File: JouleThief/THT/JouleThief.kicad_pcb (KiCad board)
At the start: 2 copper layers, 55.3 x 13.2 mm, 11 parts, among them J1 Screw_Terminal_01x02, J2 Screw_Terminal_01x02, Q1 BC547, Q2 BC547

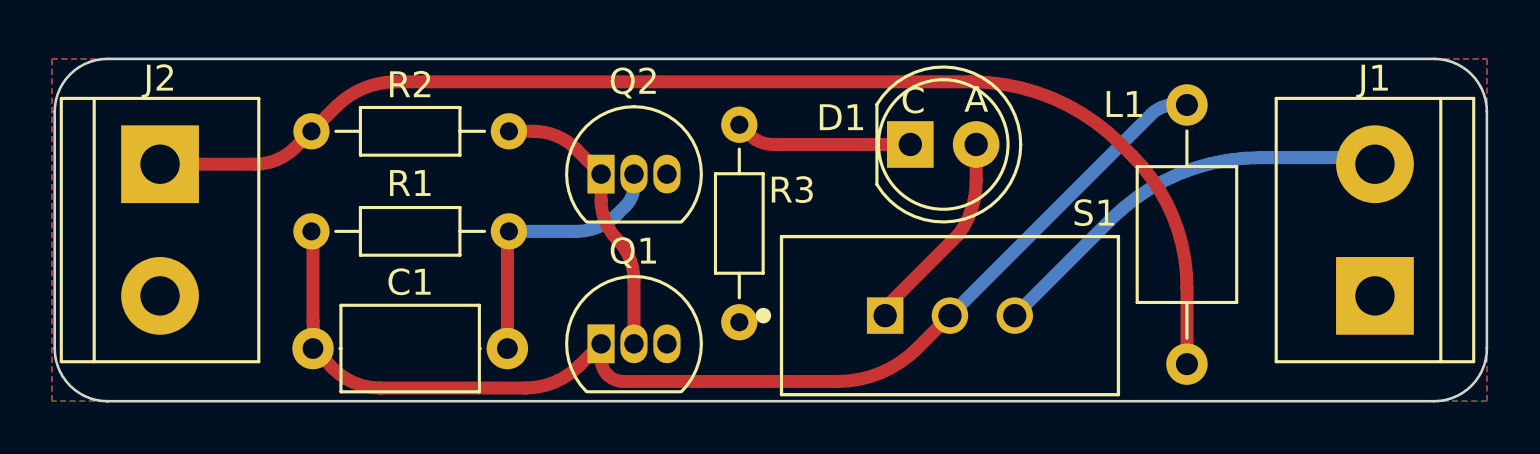
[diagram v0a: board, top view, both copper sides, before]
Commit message: added tht components back tot tht
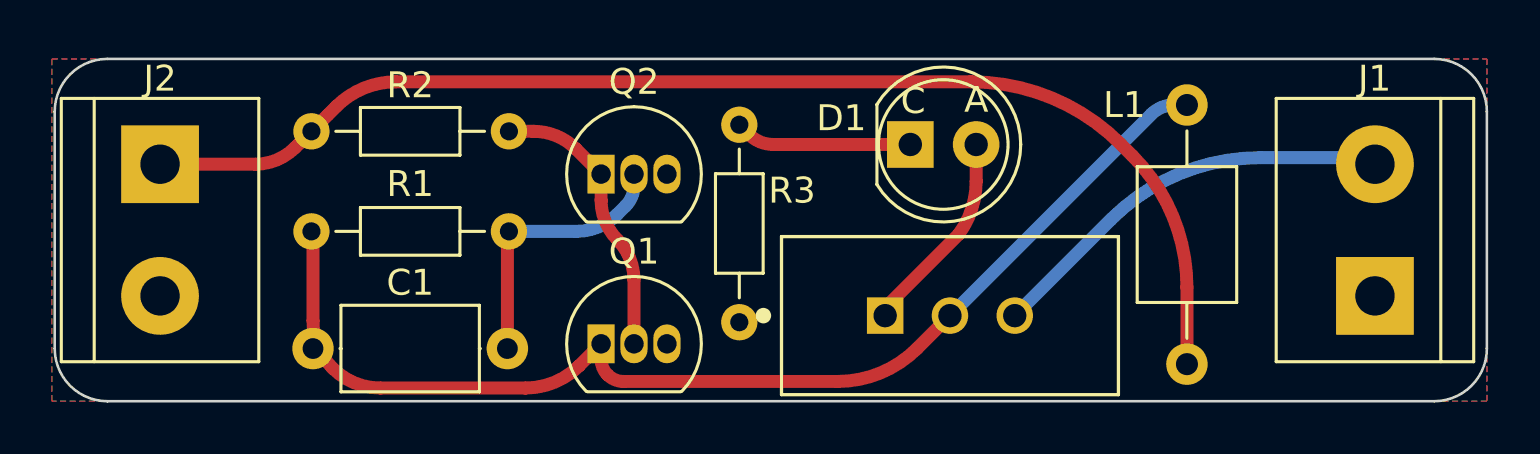
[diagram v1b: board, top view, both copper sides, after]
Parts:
- C1: value 220pf -> 100pF
- L1: value 100uH -> 220uH
- R3: value 300 -> 330
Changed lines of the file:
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@@
       (effects (font (size 1 1) (thickness 0.15)))
     )
-    (fp_text value "220pf" (at 3.75 2.67) (layer "F.Fab")
+    (fp_text value "100pF" (at 3.75 2.67) (layer "F.Fab")
       (effects (font (size 1 1) (thickness 0.15)))
     )
@@
       (effects (font (size 1 1) (thickness 0.15)))
     )
-    (fp_text value "100uH" (at 1.25 0) (layer "F.Fab")
+    (fp_text value "220uH" (at 1.25 0) (layer "F.Fab")
       (effects (font (size 1 1) (thickness 0.15)))
     )
@@
     (property "Sheetname" "")
     (attr through_hole)
-    (fp_text reference "S1" (at 5.588 -3.937) (layer "F.SilkS")
+    (fp_text reference "S1" (at 5.588 -3.937) (layer "F.SilkS") hide
       (effects (font (size 1.000685 1.000685) (thickness 0.15)))
     )
@@
       (effects (font (size 1 1) (thickness 0.15)))
     )
-    (fp_text value "300" (at 3.81 1.92 90) (layer "F.Fab")
-      (effects (font (size 1 1) (thickness 0.15)))
-    )
+    (fp_text value "330" (at 3.81 1.92 90) (layer "F.Fab")
+      (effects (font (size 1 1) (thickness 0.15)))
+    )
